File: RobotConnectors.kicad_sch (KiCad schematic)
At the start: 62 parts, among them J1 Conn_02x11_Top_Bottom, J10 Conn_01x05, J11 Conn_01x03_Male, J12 Conn_01x03_Male, J13 Conn_01x03_Male, J14 Conn_01x03_Male, J17 Conn_01x02, J18 Conn_01x02, J19 Conn_01x04, J2 Conn_02x04_Top_Bottom, J21 Conn_01x05, J27 Conn_01x03_Male, J28 Conn_01x03_Male, J29 Conn_01x03_Male, J3 Conn_01x02, J30 Conn_01x03_Male, J4 Conn_01x04, J5 Conn_01x04, J6 Conn_01x04, J7 Conn_01x04, J8 Conn_01x04, J9 Conn_01x04, U11 TXS0108EPW, U12 TXS0108EPW, U14 Fuse Holder, U15 Fuse Holder, U16 Fuse Holder, U17 Fuse Holder, U2 TPS2065CDBV

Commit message: added D3, fixed 3d model
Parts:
- added D3: SS54, Diode_SMD:D_SMA, symbol Device:D_Schottky
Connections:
- net BATTERY_CHARGE_INPUT: now also D3.1 (K)
- net V_BATTERY: now also D3.2 (A)
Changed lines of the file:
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@@
 	)
 	(junction
+		(at 168.91 87.63)
+		(diameter 0)
+		(color 0 0 0 0)
+	)
+	(junction
 		(at 167.64 152.4)
 		(diameter 0)
@@
 	(wire
 		(pts
+			(xy 168.91 87.63) (xy 168.91 95.25)
+		)
+		(stroke
+			(width 0)
+			(type default)
+		)
+	)
+	(wire
+		(pts
 			(xy 161.29 41.91) (xy 161.29 40.64)
 		)
@@
 	(wire
 		(pts
+			(xy 175.26 90.17) (xy 175.26 87.63)
+		)
+		(stroke
+			(width 0)
+			(type default)
+		)
+	)
+	(wire
+		(pts
 			(xy 140.97 74.93) (xy 142.24 74.93)
 		)
@@
 	(wire
 		(pts
+			(xy 175.26 97.79) (xy 175.26 100.33)
+		)
+		(stroke
+			(width 0)
+			(type default)
+		)
+	)
+	(wire
+		(pts
+			(xy 175.26 87.63) (xy 168.91 87.63)
+		)
+		(stroke
+			(width 0)
+			(type default)
+		)
+	)
+	(wire
+		(pts
 			(xy 53.34 71.12) (xy 85.09 71.12)
 		)
@@
 	(wire
 		(pts
-			(xy 168.91 83.82) (xy 168.91 95.25)
+			(xy 168.91 83.82) (xy 168.91 87.63)
 		)
 		(stroke
@@
 					(unit 1)
 				)
+			)
+		)
+	)
+	(symbol
+		(lib_id "Device:D_Schottky")
+		(at 175.26 93.98 270)
+		(unit 1)
+		(exclude_from_sim no)
+		(in_bom yes)
+		(on_board yes)
+		(dnp no)
+		(fields_autoplaced yes)
+		(property "Reference" "D3"
+			(at 177.8 92.3924 90)
+			(effects
+				(font
+					(size 1.27 1.27)
+				)
+				(justify left)
+			)
+		)
+		(property "Value" "SS54"
+			(at 177.8 94.9324 90)
+			(effects
+				(font
+					(size 1.27 1.27)
+				)
+				(justify left)
+			)
+		)
+		(property "Footprint" "Diode_SMD:D_SMA"
+			(at 175.26 93.98 0)
+			(effects
+				(font
+					(size 1.27 1.27)
+				)
+				(hide yes)
+			)
+		)
+		(property "Datasheet" "~"
+			(at 175.26 93.98 0)
+			(effects
+				(font
+					(size 1.27 1.27)
+				)
+				(hide yes)
+			)
+		)
+		(property "Description" ""
+			(at 175.26 93.98 0)
+			(effects
+				(font
+					(size 1.27 1.27)
+				)
+				(hide yes)
+			)
+		)
+		(property "Digikey" "3757-SB54AFC_R1_00001CT-ND"
+			(at 175.26 93.98 0)
+			(effects
+				(font
+					(size 1.27 1.27)
+				)
+				(hide yes)
+			)
+		)
+		(property "Part Number" "SB54AFC_R1_00001"
+			(at 175.26 93.98 0)
+			(effects
+				(font
+					(size 1.27 1.27)
+				)
+				(hide yes)
+			)
+		)
+		(property "Stock_PN" "D-SMA-Schottky-40V-5A"
+			(at 175.26 93.98 0)
+			(effects
+				(font
+					(size 1.27 1.27)
+				)
+				(hide yes)
+			)
+		)
+		(property "LCSC" ""
+			(at 175.26 93.98 0)
+			(effects
+				(font
+					(size 1.27 1.27)
+				)
+				(hide yes)
+			)
+		)
+		(property "JLC" "C22452"
+			(at 175.26 93.98 0)
+			(effects
+				(font
+					(size 1.27 1.27)
+				)
+				(hide yes)
+			)
+		)
+		(pin "1"
+		)
+		(pin "2"
+		)
+		(instances
+			(project "hw-openmower-yardforce"
+				(path "/e12e8a63-1d1b-4736-9aba-a87a258b2b11/7a7dfcf0-39e0-4eb7-9f4b-f66d7afbe41f"
+					(reference "D3")
+					(unit 1)
+				)

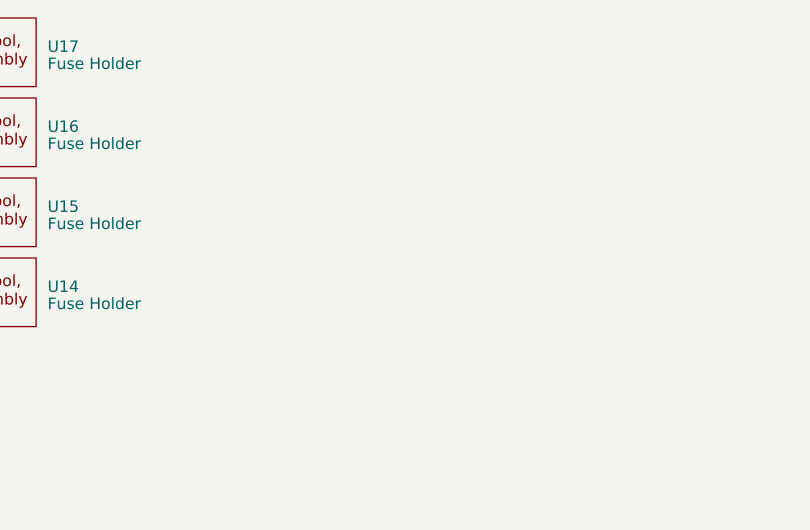
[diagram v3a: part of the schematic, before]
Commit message: Added Fuses
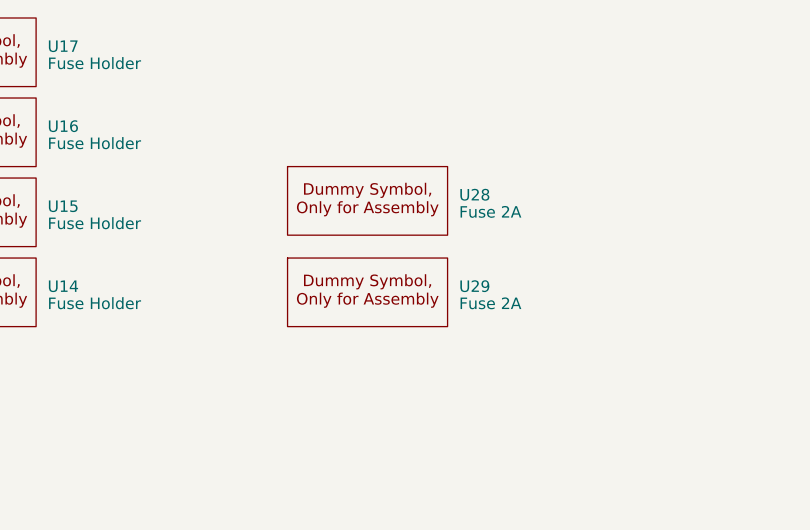
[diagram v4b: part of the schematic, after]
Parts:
- added U28, U29: Fuse 2A, xtech:Dummy, symbol xtech:Dummy
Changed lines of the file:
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@@
 	)
 	(symbol
+		(lib_id "xtech:Dummy")
+		(at 224.79 -2.54 0)
+		(unit 1)
+		(exclude_from_sim no)
+		(in_bom yes)
+		(on_board yes)
+		(dnp no)
+		(fields_autoplaced yes)
+		(property "Reference" "U29"
+			(at 243.84 -6.9851 0)
+			(effects
+				(font
+					(size 1.27 1.27)
+				)
+				(justify left)
+			)
+		)
+		(property "Value" "Fuse 2A"
+			(at 243.84 -5.08 0)
+			(effects
+				(font
+					(size 1.27 1.27)
+				)
+				(justify left)
+			)
+		)
+		(property "Footprint" "xtech:Dummy"
+			(at 224.79 -2.54 0)
+			(effects
+				(font
+					(size 1.27 1.27)
+				)
+				(hide yes)
+			)
+		)
+		(property "Datasheet" ""
+			(at 224.79 -2.54 0)
+			(effects
+				(font
+					(size 1.27 1.27)
+				)
+				(hide yes)
+			)
+		)
+		(property "Description" ""
+			(at 224.79 -2.54 0)
+			(effects
+				(font
+					(size 1.27 1.27)
+				)
+				(hide yes)
+			)
+		)
+		(property "JLC" "C356459"
+			(at 224.79 -2.54 0)
+			(effects
+				(font
+					(size 1.27 1.27)
+				)
+				(hide yes)
+			)
+		)
+		(property "Height" ""
+			(at 224.79 -2.54 0)
+			(effects
+				(font
+					(size 1.27 1.27)
+				)
+				(hide yes)
+			)
+		)
+		(property "Manufacturer_Name" ""
+			(at 224.79 -2.54 0)
+			(effects
+				(font
+					(size 1.27 1.27)
+				)
+				(hide yes)
+			)
+		)
+		(property "Manufacturer_Part_Number" ""
+			(at 224.79 -2.54 0)
+			(effects
+				(font
+					(size 1.27 1.27)
+				)
+				(hide yes)
+			)
+		)
+		(property "Mouser Part Number" ""
+			(at 224.79 -2.54 0)
+			(effects
+				(font
+					(size 1.27 1.27)
+				)
+				(hide yes)
+			)
+		)
+		(property "Mouser Price/Stock" ""
+			(at 224.79 -2.54 0)
+			(effects
+				(font
+					(size 1.27 1.27)
+				)
+				(hide yes)
+			)
+		)
+		(instances
+			(project "hw-openmower-yardforce"
+				(path "/e12e8a63-1d1b-4736-9aba-a87a258b2b11/7a7dfcf0-39e0-4eb7-9f4b-f66d7afbe41f"
+					(reference "U29")
+					(unit 1)
+				)
+			)
+		)
+	)
+	(symbol
 		(lib_id "Device:R")
 		(at 129.54 146.05 0)
@@
 					(unit 1)
 				)
+			)
+		)
+	)
+	(symbol
+		(lib_id "xtech:Dummy")
+		(at 224.79 -12.7 0)
+		(unit 1)
+		(exclude_from_sim no)
+		(in_bom yes)
+		(on_board yes)
+		(dnp no)
+		(fields_autoplaced yes)
+		(property "Reference" "U28"
+			(at 243.84 -17.1451 0)
+			(effects
+				(font
+					(size 1.27 1.27)
+				)
+				(justify left)
+			)
+		)
+		(property "Value" "Fuse 2A"
+			(at 243.84 -15.24 0)
+			(effects
+				(font
+					(size 1.27 1.27)
+				)
+				(justify left)
+			)
+		)
+		(property "Footprint" "xtech:Dummy"
+			(at 224.79 -12.7 0)
+			(effects
+				(font
+					(size 1.27 1.27)
+				)
+				(hide yes)
+			)
+		)
+		(property "Datasheet" ""
+			(at 224.79 -12.7 0)
+			(effects
+				(font
+					(size 1.27 1.27)
+				)
+				(hide yes)
+			)
+		)
+		(property "Description" ""
+			(at 224.79 -12.7 0)
+			(effects
+				(font
+					(size 1.27 1.27)
+				)
+				(hide yes)
+			)
+		)
+		(property "JLC" "C356459"
+			(at 224.79 -12.7 0)
+			(effects
+				(font
+					(size 1.27 1.27)
+				)
+				(hide yes)
+			)
+		)
+		(property "Height" ""
+			(at 224.79 -12.7 0)
+			(effects
+				(font
+					(size 1.27 1.27)
+				)
+				(hide yes)
+			)
+		)
+		(property "Manufacturer_Name" ""
+			(at 224.79 -12.7 0)
+			(effects
+				(font
+					(size 1.27 1.27)
+				)
+				(hide yes)
+			)
+		)
+		(property "Manufacturer_Part_Number" ""
+			(at 224.79 -12.7 0)
+			(effects
+				(font
+					(size 1.27 1.27)
+				)
+				(hide yes)
+			)
+		)
+		(property "Mouser Part Number" ""
+			(at 224.79 -12.7 0)
+			(effects
+				(font
+					(size 1.27 1.27)
+				)
+				(hide yes)
+			)
+		)
+		(property "Mouser Price/Stock" ""
+			(at 224.79 -12.7 0)
+			(effects
+				(font
+					(size 1.27 1.27)
+				)
+				(hide yes)
+			)
+		)
+		(instances
+			(project "hw-openmower-yardforce"
+				(path "/e12e8a63-1d1b-4736-9aba-a87a258b2b11/7a7dfcf0-39e0-4eb7-9f4b-f66d7afbe41f"
+					(reference "U28")
+					(unit 1)
+				)

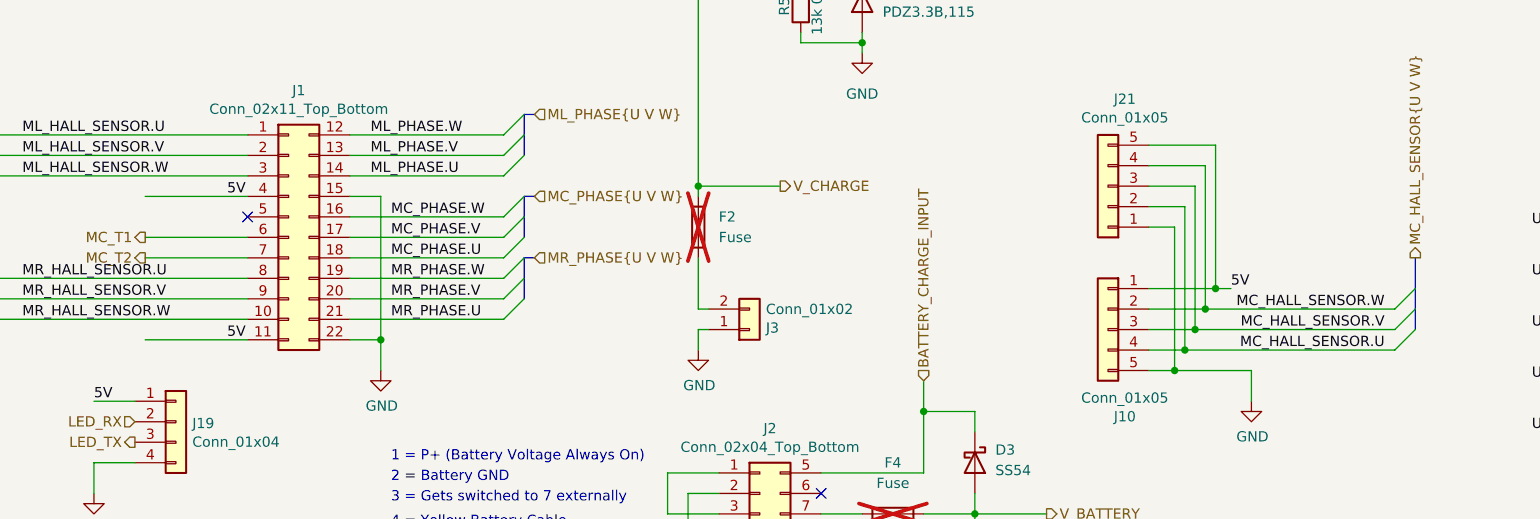
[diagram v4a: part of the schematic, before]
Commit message: Make ERC happy
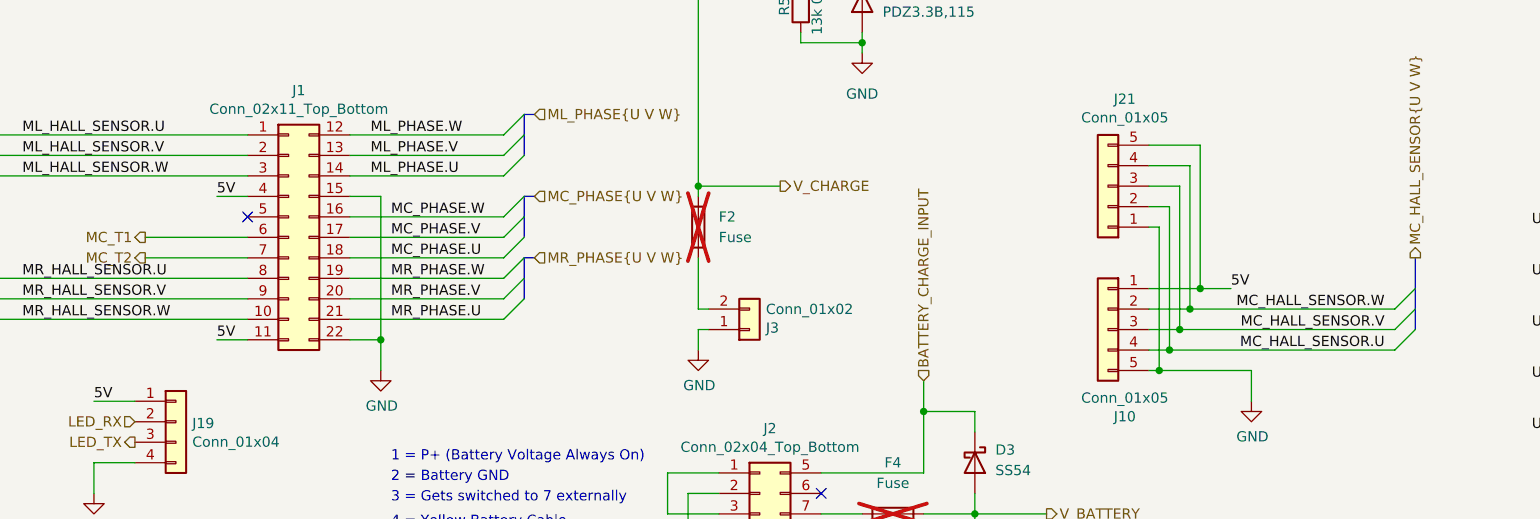
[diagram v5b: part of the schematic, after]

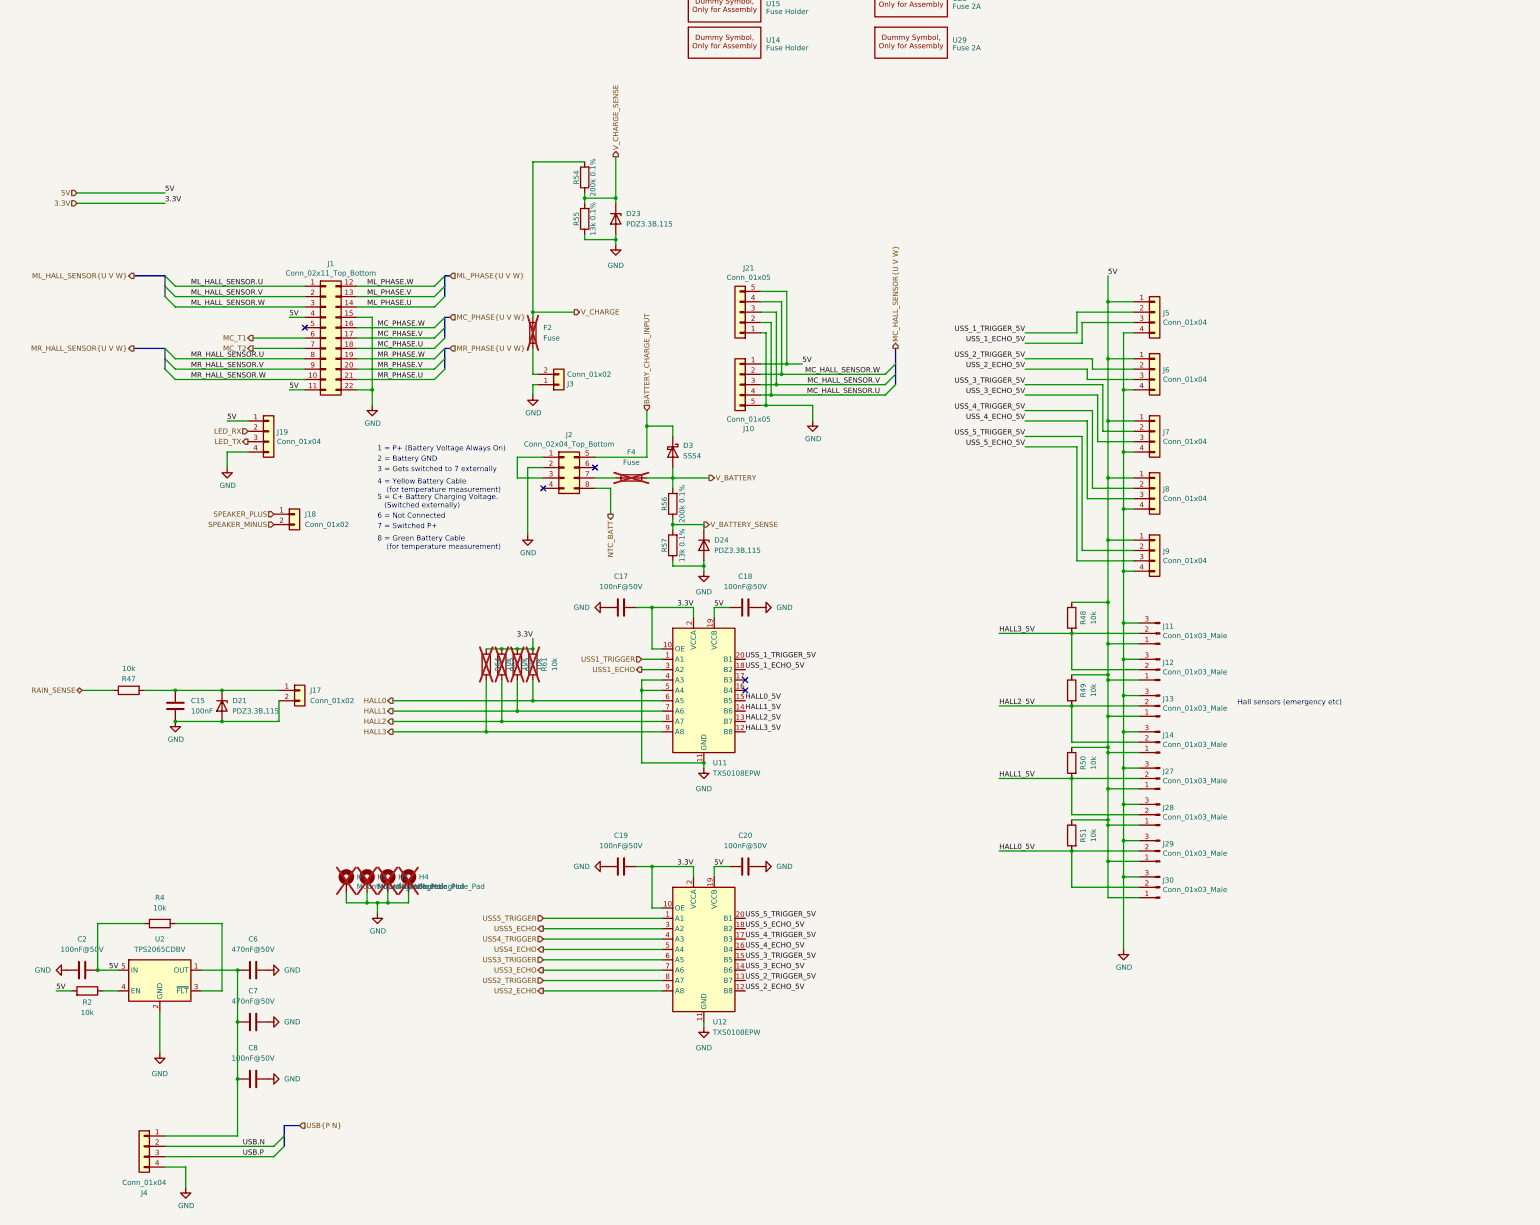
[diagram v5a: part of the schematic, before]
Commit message: Fix V_CHARGE ADC
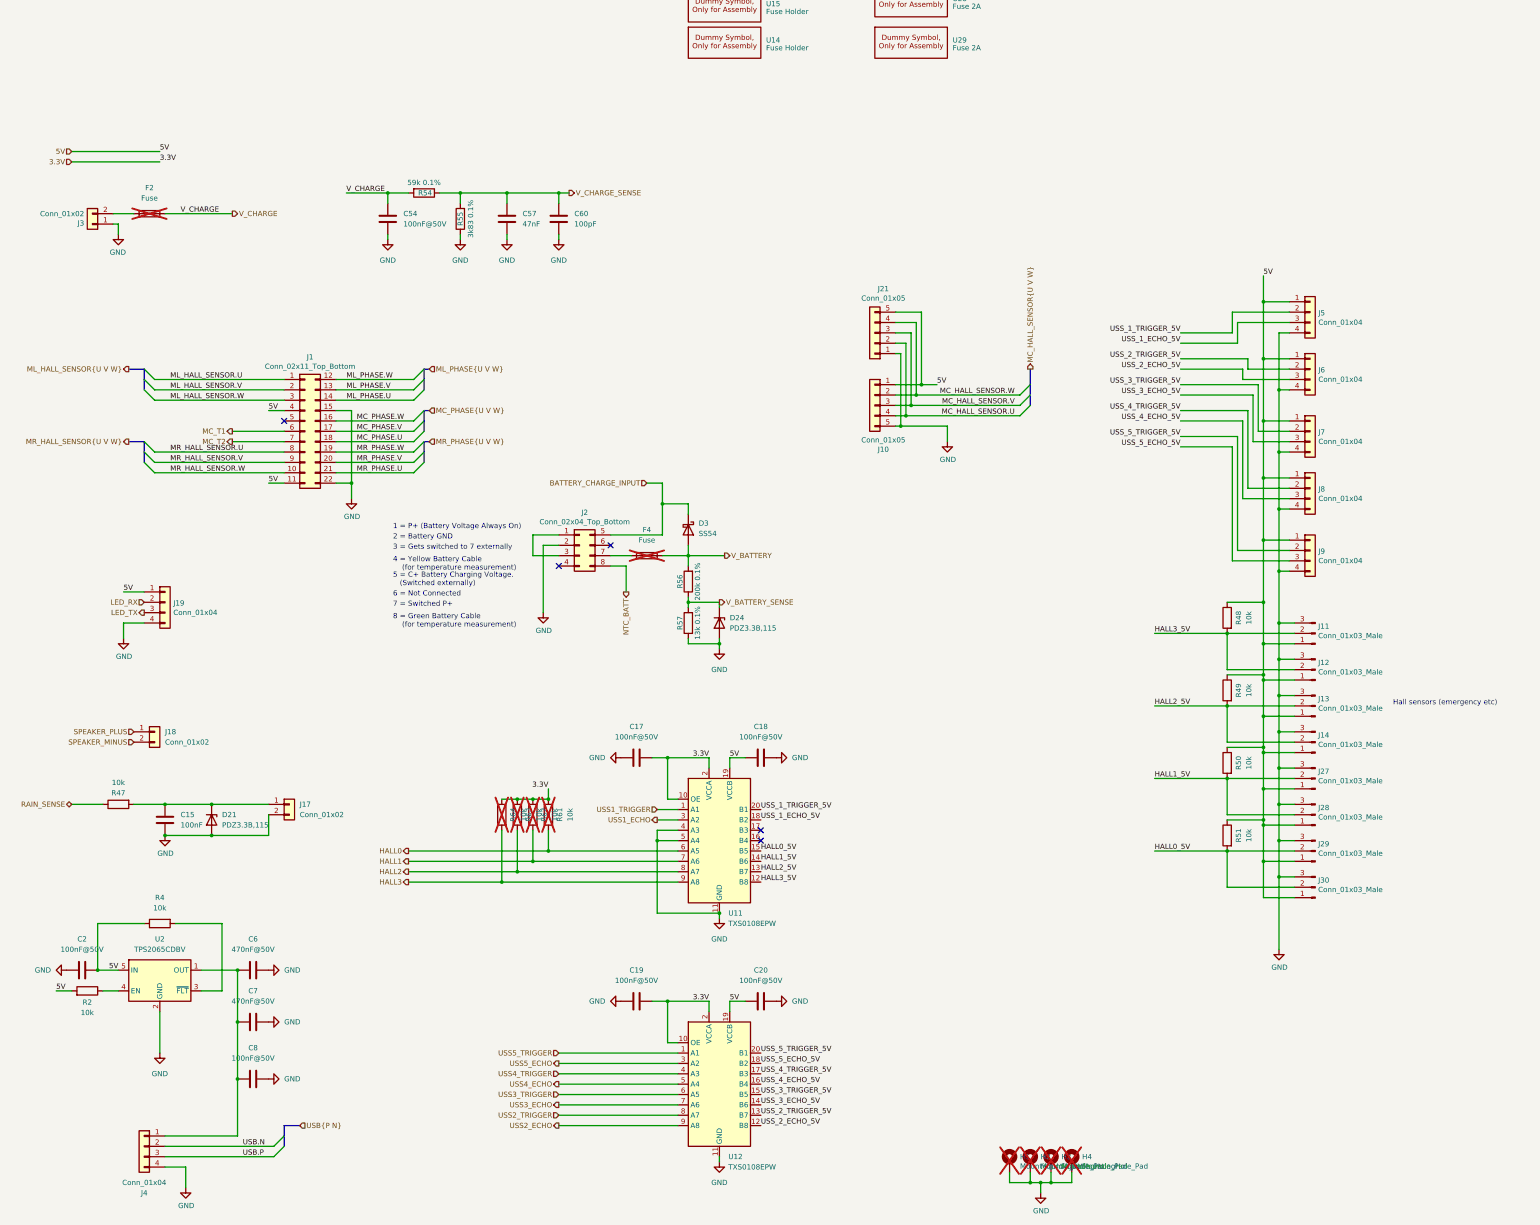
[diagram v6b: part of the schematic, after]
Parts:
- removed D23: PDZ3.3B,115, Diode_SMD:D_SOD-323, symbol Device:D_Zener
- added C54: 100nF@50V, Capacitor_SMD:C_0402_1005Metric, symbol Device:C
- added C57: 47nF, Capacitor_SMD:C_0603_1608Metric, symbol Device:C
- added C60: 100pF, Capacitor_SMD:C_0402_1005Metric, symbol Device:C
- R54: value 200k 0.1% -> 59k 0.1%; JLC C728556 -> C852853
- R55: value 13k 0.1% -> 3k83 0.1%; JLC C852524 -> C852772
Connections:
- net GND: now also C54.2, C57.2, C60.2
- net V_CHARGE: now also C54.1
- net V_CHARGE_SENSE: now also C57.1, C60.1
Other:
- moved on the sheet: C15, C17, C18, C19, C20, D21, D24, D3, F2, F4, H1, H2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
